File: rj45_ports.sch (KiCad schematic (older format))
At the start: 24 parts, among them J1 BEL_0845_2G1T_H5, U2 74LVC1G06, U6 74LVC1G06

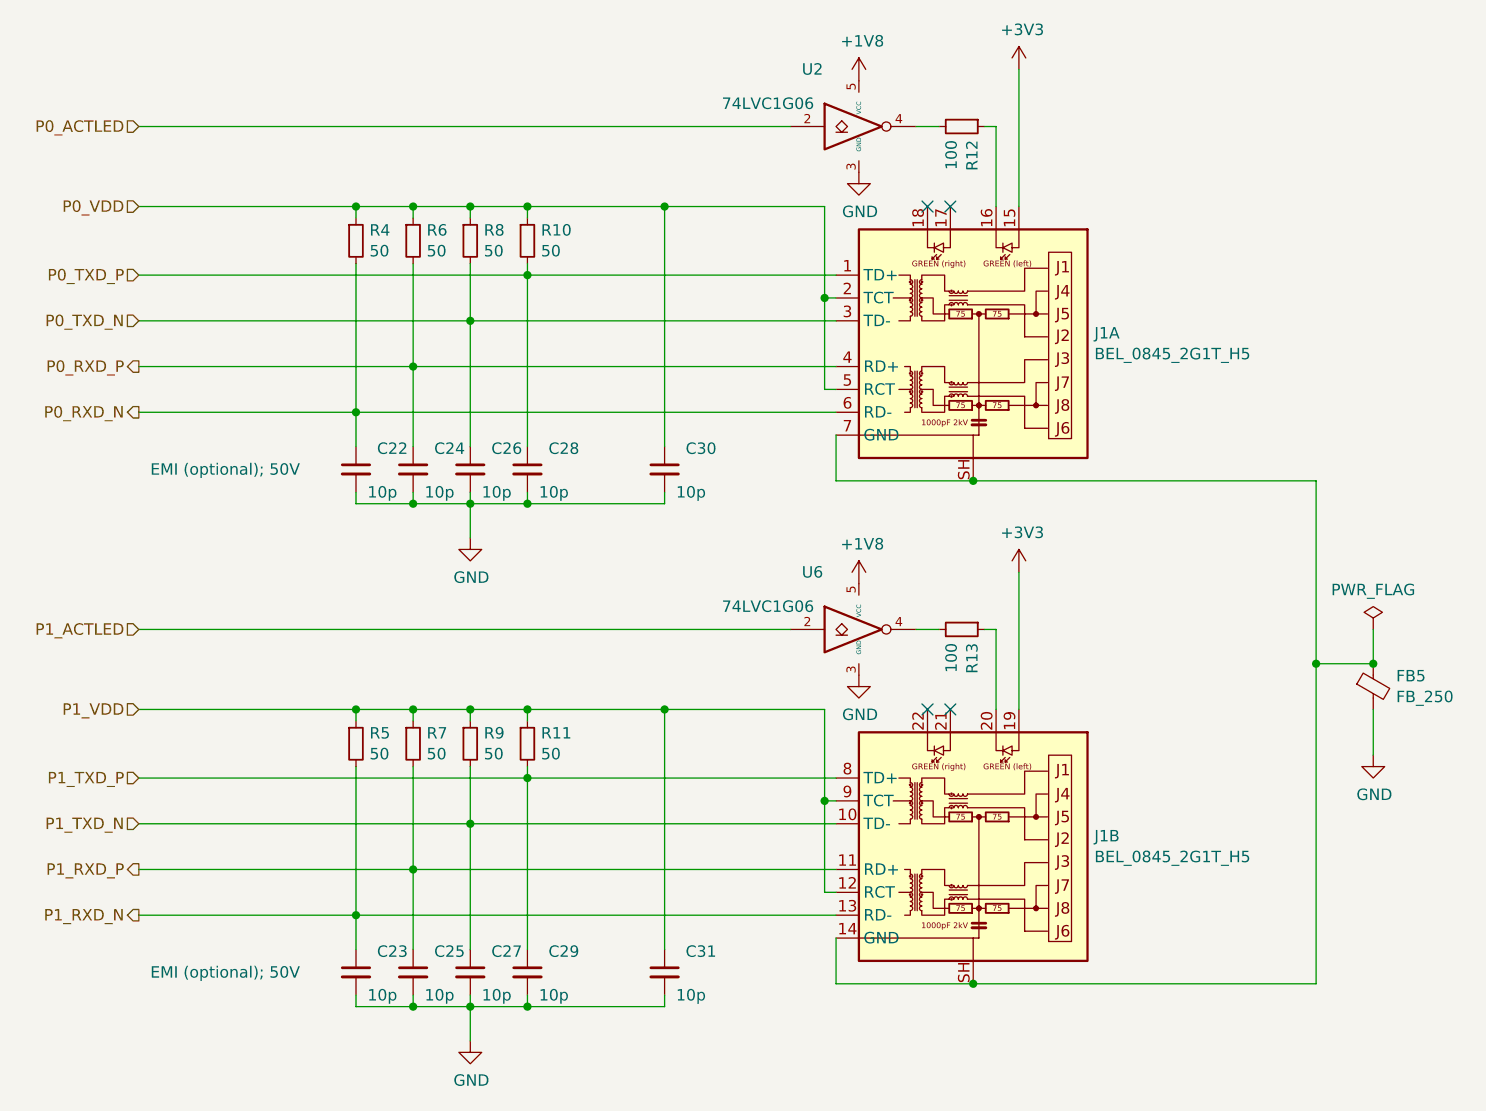
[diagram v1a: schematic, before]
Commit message: reannotated for merging with te0715 development board
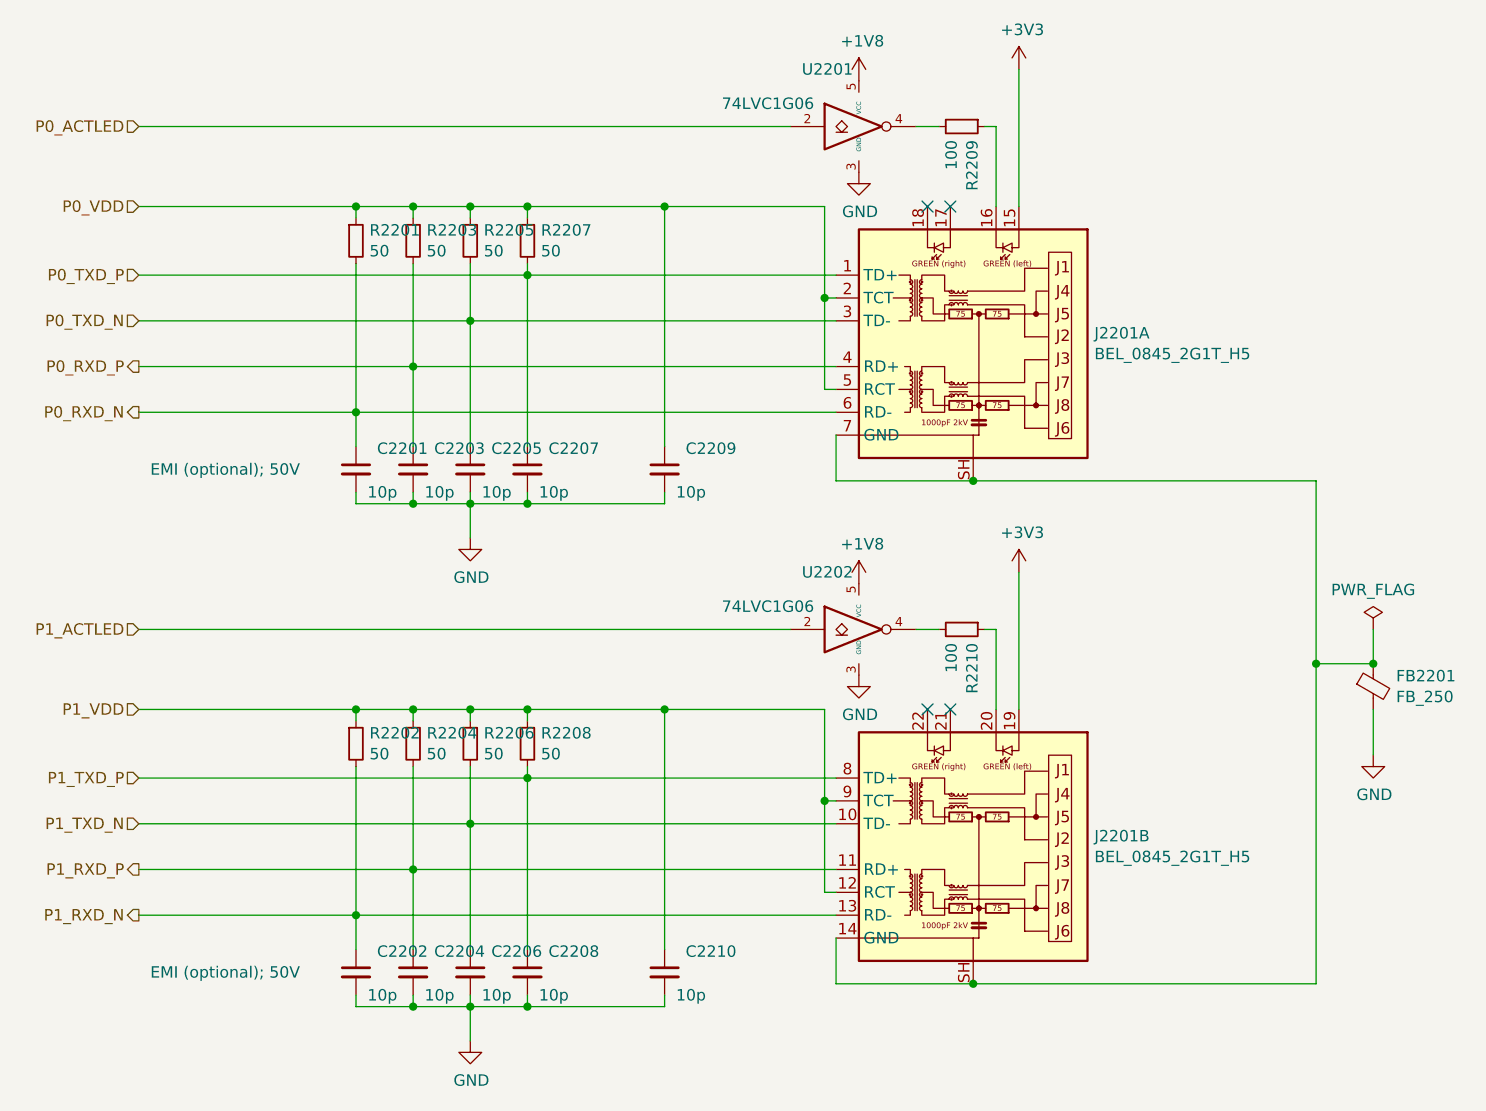
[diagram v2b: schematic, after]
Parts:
- renumbered C22 to C2201, C23 to C2202, C24 to C2203, C25 to C2204, C26 to C2205, C27 to C2206, C28 to C2207, C29 to C2208, C30 to C2209, C31 to C2210, FB5 to FB2201, J1 to J2201, R4 to R2201, R5 to R2202, R6 to R2203, R7 to R2204, R8 to R2205, R9 to R2206, R10 to R2207, R11 to R2208, R12 to R2209, R13 to R2210, U2 to U2201, U6 to U2202
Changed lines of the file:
@@
 $EndDescr
 $Comp
-L fmc:BEL_0845_2G1T_H5 J1
+L fmc:BEL_0845_2G1T_H5 J2201
 U 1 1 60DC2D2D
 P 5400 2300
-F 0 "J1" H 4870 2346 50  0000 R CNN
+F 0 "J2201" H 4870 2346 50  0000 R CNN
 F 1 "BEL_0845_2G1T_H5" H 4870 2255 50  0000 R CNN
 F 2 "proj_footprints:BEL_0845-2G1T-H5" H 5400 1550 50  0001 C CNN
@@
 Connection ~ 5400 2900
 $Comp
-L Device:Ferrite_Bead_Small FB5
+L Device:Ferrite_Bead_Small FB2201
 U 1 1 60DCCC48
 P 7150 3800
-F 0 "FB5" H 7250 3846 50  0000 L CNN
+F 0 "FB2201" H 7250 3846 50  0000 L CNN
 F 1 "FB_250" H 7250 3755 50  0000 L CNN
 F 2 "Inductor_SMD:L_0603_1608Metric" V 7080 3800 50  0001 C CNN
@@
 	7150 3900 7150 4100
 $Comp
-L Device:R_Small R8
+L Device:R_Small R2205
 U 1 1 60DCE62D
 P 3200 1850
-F 0 "R8" H 3259 1896 50  0000 L CNN
+F 0 "R2205" H 3259 1896 50  0000 L CNN
 F 1 "50" H 3259 1805 50  0000 L CNN
 F 2 "Resistor_SMD:R_0402_1005Metric" H 3200 1850 50  0001 C CNN
@@
 $EndComp
 $Comp
-L Device:R_Small R10
+L Device:R_Small R2207
 U 1 1 60DCE9EC
 P 3450 1850
-F 0 "R10" H 3509 1896 50  0000 L CNN
+F 0 "R2207" H 3509 1896 50  0000 L CNN
 F 1 "50" H 3509 1805 50  0000 L CNN
 F 2 "Resistor_SMD:R_0402_1005Metric" H 3450 1850 50  0001 C CNN
@@
 $EndComp
 $Comp
-L Device:R_Small R6
+L Device:R_Small R2203
 U 1 1 60DCEBD5
 P 2950 1850
-F 0 "R6" H 3009 1896 50  0000 L CNN
+F 0 "R2203" H 3009 1896 50  0000 L CNN
 F 1 "50" H 3009 1805 50  0000 L CNN
 F 2 "Resistor_SMD:R_0402_1005Metric" H 2950 1850 50  0001 C CNN
@@
 $EndComp
 $Comp
-L Device:R_Small R4
+L Device:R_Small R2201
 U 1 1 60DCEDD7
 P 2700 1850
-F 0 "R4" H 2759 1896 50  0000 L CNN
+F 0 "R2201" H 2759 1896 50  0000 L CNN
 F 1 "50" H 2759 1805 50  0000 L CNN
 F 2 "Resistor_SMD:R_0402_1005Metric" H 2700 1850 50  0001 C CNN
@@
 	2700 2600 4800 2600
 $Comp
-L Device:C_Small C22
+L Device:C_Small C2201
 U 1 1 60DD356A
 P 2700 2850
-F 0 "C22" H 2792 2941 50  0000 L CNN
+F 0 "C2201" H 2792 2941 50  0000 L CNN
 F 1 "10p" H 2750 2750 50  0000 L CNN
 F 2 "Capacitor_SMD:C_0402_1005Metric" H 2700 2850 50  0001 C CNN
@@
 $EndComp
 $Comp
-L Device:C_Small C24
+L Device:C_Small C2203
 U 1 1 60DD40A0
 P 2950 2850
-F 0 "C24" H 3042 2941 50  0000 L CNN
+F 0 "C2203" H 3042 2941 50  0000 L CNN
 F 1 "10p" H 3000 2750 50  0000 L CNN
 F 2 "Capacitor_SMD:C_0402_1005Metric" H 2950 2850 50  0001 C CNN
@@
 Connection ~ 3450 2000
 $Comp
-L Device:C_Small C26
+L Device:C_Small C2205
 U 1 1 60DD720F
 P 3200 2850
-F 0 "C26" H 3292 2941 50  0000 L CNN
+F 0 "C2205" H 3292 2941 50  0000 L CNN
 F 1 "10p" H 3250 2750 50  0000 L CNN
 F 2 "Capacitor_SMD:C_0402_1005Metric" H 3200 2850 50  0001 C CNN
@@
 $EndComp
 $Comp
-L Device:C_Small C28
+L Device:C_Small C2207
 U 1 1 60DD7536
 P 3450 2850
-F 0 "C28" H 3542 2941 50  0000 L CNN
+F 0 "C2207" H 3542 2941 50  0000 L CNN
 F 1 "10p" H 3500 2750 50  0000 L CNN
 F 2 "Capacitor_SMD:C_0402_1005Metric" H 3450 2850 50  0001 C CNN
@@
 $EndComp
 $Comp
-L Device:C_Small C30
+L Device:C_Small C2209
 U 1 1 60DD78C3
 P 4050 2850
-F 0 "C30" H 4142 2941 50  0000 L CNN
+F 0 "C2209" H 4142 2941 50  0000 L CNN
 F 1 "10p" H 4100 2750 50  0000 L CNN
 F 2 "Capacitor_SMD:C_0402_1005Metric" H 4050 2850 50  0001 C CNN
@@
 $EndComp
 $Comp
-L Device:R_Small R12
+L Device:R_Small R2209
 U 1 1 60E01790
 P 5350 1350
-F 0 "R12" H 5409 1396 50  0000 L CNN
+F 0 "R2209" H 5409 1396 50  0000 L CNN
 F 1 "100" H 5409 1305 50  0000 L CNN
 F 2 "Resistor_SMD:R_0603_1608Metric" H 5350 1350 50  0001 C CNN
@@
 Connection ~ 2700 1700
 $Comp
-L fmc:BEL_0845_2G1T_H5 J1
+L fmc:BEL_0845_2G1T_H5 J2201
 U 2 1 60E19485
 P 5400 4500
-F 0 "J1" H 4870 4546 50  0000 R CNN
+F 0 "J2201" H 4870 4546 50  0000 R CNN
 F 1 "BEL_0845_2G1T_H5" H 4870 4455 50  0000 R CNN
 F 2 "proj_footprints:BEL_0845-2G1T-H5" H 5400 3750 50  0001 C CNN
@@
 Connection ~ 5400 5100
 $Comp
-L Device:R_Small R9
+L Device:R_Small R2206
 U 1 1 60E197D6
 P 3200 4050
-F 0 "R9" H 3259 4096 50  0000 L CNN
+F 0 "R2206" H 3259 4096 50  0000 L CNN
 F 1 "50" H 3259 4005 50  0000 L CNN
 F 2 "Resistor_SMD:R_0402_1005Metric" H 3200 4050 50  0001 C CNN
@@
 $EndComp
 $Comp
-L Device:R_Small R11
+L Device:R_Small R2208
 U 1 1 60E197E0
 P 3450 4050
-F 0 "R11" H 3509 4096 50  0000 L CNN
+F 0 "R2208" H 3509 4096 50  0000 L CNN
 F 1 "50" H 3509 4005 50  0000 L CNN
 F 2 "Resistor_SMD:R_0402_1005Metric" H 3450 4050 50  0001 C CNN
@@
 $EndComp
 $Comp
-L Device:R_Small R7
+L Device:R_Small R2204
 U 1 1 60E197EA
 P 2950 4050
-F 0 "R7" H 3009 4096 50  0000 L CNN
+F 0 "R2204" H 3009 4096 50  0000 L CNN
 F 1 "50" H 3009 4005 50  0000 L CNN
 F 2 "Resistor_SMD:R_0402_1005Metric" H 2950 4050 50  0001 C CNN
@@
 $EndComp
 $Comp
-L Device:R_Small R5
+L Device:R_Small R2202
 U 1 1 60E197F4
 P 2700 4050
-F 0 "R5" H 2759 4096 50  0000 L CNN
+F 0 "R2202" H 2759 4096 50  0000 L CNN
 F 1 "50" H 2759 4005 50  0000 L CNN
 F 2 "Resistor_SMD:R_0402_1005Metric" H 2700 4050 50  0001 C CNN
@@
 	2700 4800 4800 4800
 $Comp
-L Device:C_Small C23
+L Device:C_Small C2202
 U 1 1 60E19817
 P 2700 5050
-F 0 "C23" H 2792 5141 50  0000 L CNN
+F 0 "C2202" H 2792 5141 50  0000 L CNN
 F 1 "10p" H 2750 4950 50  0000 L CNN
 F 2 "Capacitor_SMD:C_0402_1005Metric" H 2700 5050 50  0001 C CNN
@@
 $EndComp
 $Comp
-L Device:C_Small C25
+L Device:C_Small C2204
 U 1 1 60E19822
 P 2950 5050
-F 0 "C25" H 3042 5141 50  0000 L CNN
+F 0 "C2204" H 3042 5141 50  0000 L CNN
 F 1 "10p" H 3000 4950 50  0000 L CNN
 F 2 "Capacitor_SMD:C_0402_1005Metric" H 2950 5050 50  0001 C CNN
@@
 Connection ~ 3450 4200
 $Comp
-L Device:C_Small C27
+L Device:C_Small C2206
 U 1 1 60E19835
 P 3200 5050
-F 0 "C27" H 3292 5141 50  0000 L CNN
+F 0 "C2206" H 3292 5141 50  0000 L CNN
 F 1 "10p" H 3250 4950 50  0000 L CNN
 F 2 "Capacitor_SMD:C_0402_1005Metric" H 3200 5050 50  0001 C CNN
@@
 $EndComp
 $Comp
-L Device:C_Small C29
+L Device:C_Small C2208
 U 1 1 60E19840
 P 3450 5050
-F 0 "C29" H 3542 5141 50  0000 L CNN
+F 0 "C2208" H 3542 5141 50  0000 L CNN
 F 1 "10p" H 3500 4950 50  0000 L CNN
 F 2 "Capacitor_SMD:C_0402_1005Metric" H 3450 5050 50  0001 C CNN
@@
 $EndComp
 $Comp
-L Device:C_Small C31
+L Device:C_Small C2210
 U 1 1 60E1984B
 P 4050 5050
-F 0 "C31" H 4142 5141 50  0000 L CNN
+F 0 "C2210" H 4142 5141 50  0000 L CNN
 F 1 "10p" H 4100 4950 50  0000 L CNN
 F 2 "Capacitor_SMD:C_0402_1005Metric" H 4050 5050 50  0001 C CNN
@@
 $EndComp
 $Comp
-L Device:R_Small R13
+L Device:R_Small R2210
 U 1 1 60E19870
 P 5350 3550
-F 0 "R13" H 5409 3596 50  0000 L CNN
+F 0 "R2210" H 5409 3596 50  0000 L CNN
 F 1 "100" H 5409 3505 50  0000 L CNN
 F 2 "Resistor_SMD:R_0603_1608Metric" H 5350 3550 50  0001 C CNN
@@
 Connection ~ 7150 3700
 $Comp
-L fmc:74LVC1G06 U2
+L fmc:74LVC1G06 U2201
 U 1 1 61143898
 P 4900 1350
-F 0 "U2" H 4650 1600 50  0000 L CNN
+F 0 "U2201" H 4650 1600 50  0000 L CNN
 F 1 "74LVC1G06" H 4300 1450 50  0000 L CNN
 F 2 "Package_TO_SOT_SMD:SOT-553" H 4900 1350 50  0001 C CNN
@@
 $EndComp
 $Comp
-L fmc:74LVC1G06 U6
+L fmc:74LVC1G06 U2202
 U 1 1 61157A24
 P 4900 3550
-F 0 "U6" H 4650 3800 50  0000 L CNN
+F 0 "U2202" H 4650 3800 50  0000 L CNN
 F 1 "74LVC1G06" H 4300 3650 50  0000 L CNN
 F 2 "Package_TO_SOT_SMD:SOT-553" H 4900 3550 50  0001 C CNN
